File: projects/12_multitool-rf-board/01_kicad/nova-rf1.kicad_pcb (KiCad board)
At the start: 4 copper layers, 100 x 60 mm, 86 parts, among them M1 vibro, SW1 RFswitch, SW2 RFswitch, U1 STM32WB55RG, U10 ESD, U2 CC1101, U3 ST25R3916, U5 ST7565R, U6 BQ25896, U7 BQ27220, U8 LM3281, U8B LM3281, U9 loadsw, X10 BAT+NTC, X6 FFC 18p, Y1 32MHz, Y2 32.768kHz

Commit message: proj12: rename board CRL-MT1 -> NOVA-RF1 (project-wide)
Global rename across source, docs, generated schematic/board/footprint-lib,
BOM/CPL, enclosure and fab tooling. No functional change. Footprint library
prefix crl-mt1: -> nova-rf1:; silkscreen/title/fab-file names updated.
(The in-flight compact route output will be renamed when it completes.)

Co-Authored-By: Claude Opus 4.8 <noreply@anthropic.com>
Claude-Session: https://claude.ai/code/session_01Hk6s8R6up8HYVQWXd3atVk
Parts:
- ANT1: footprint crl-mt1:Antenna_Chip -> nova-rf1:Antenna_Chip
- ANT_LF: footprint crl-mt1:RFID_125k_Coil -> nova-rf1:RFID_125k_Coil
- ANT_NFC: footprint crl-mt1:NFC_Loop_Antenna -> nova-rf1:NFC_Loop_Antenna
- DA7: footprint crl-mt1:LP5562_DSBGA12 -> nova-rf1:LP5562_DSBGA12
- FLT1: footprint crl-mt1:RF_filter -> nova-rf1:RF_filter
- FLT2: footprint crl-mt1:Johanson_0310_Balun -> nova-rf1:Johanson_0310_Balun
- J_IBTN: footprint crl-mt1:iButton_Contacts -> nova-rf1:iButton_Contacts
- J_SD: footprint crl-mt1:microSD_7p -> nova-rf1:microSD_7p
- J_SWD: footprint crl-mt1:TagConnect_TC2030 -> nova-rf1:TagConnect_TC2030
- LS1: footprint crl-mt1:Speaker_2p -> nova-rf1:Speaker_2p
- M1: footprint crl-mt1:Vibro_2p -> nova-rf1:Vibro_2p
- SW1, SW2: footprint crl-mt1:RF_Switch_TSNP9 -> nova-rf1:RF_Switch_TSNP9
- U5: footprint crl-mt1:Display_ST7565_FFC -> nova-rf1:Display_ST7565_FFC
- U_IR: footprint crl-mt1:TSOP_IR_3p -> nova-rf1:TSOP_IR_3p
- VD4: footprint crl-mt1:LED_RGB_4p -> nova-rf1:LED_RGB_4p
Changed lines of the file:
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@@
 	(net 176 "unconnected-(U9-4)")
 	(net 177 "unconnected-(U9-5)")
-	(footprint "crl-mt1:Display_ST7565_FFC"
+	(footprint "nova-rf1:Display_ST7565_FFC"
 		(layer "F.Cu")
 		(at 109.739287 42.5786)
@@
 		(embedded_fonts no)
 	)
-	(footprint "crl-mt1:iButton_Contacts"
+	(footprint "nova-rf1:iButton_Contacts"
 		(layer "F.Cu")
 		(at 76.263095 43.5786)
@@
 		)
 	)
-	(footprint "crl-mt1:Speaker_2p"
+	(footprint "nova-rf1:Speaker_2p"
 		(layer "F.Cu")
 		(at 85.013095 43.0786)
@@
 		)
 	)
-	(footprint "crl-mt1:microSD_7p"
+	(footprint "nova-rf1:microSD_7p"
 		(layer "F.Cu")
 		(at 67.513095 42.6786)
@@
 		(embedded_fonts no)
 	)
-	(footprint "crl-mt1:RF_Switch_TSNP9"
+	(footprint "nova-rf1:RF_Switch_TSNP9"
 		(layer "F.Cu")
 		(at 101.318096 69.2681)
@@
 		)
 	)
-	(footprint "crl-mt1:RFID_125k_Coil"
+	(footprint "nova-rf1:RFID_125k_Coil"
 		(locked yes)
 		(layer "F.Cu")
@@
 		(embedded_fonts no)
 	)
-	(footprint "crl-mt1:LP5562_DSBGA12"
+	(footprint "nova-rf1:LP5562_DSBGA12"
 		(layer "F.Cu")
 		(at 44.396667 84.917499)
@@
 		)
 	)
-	(footprint "crl-mt1:NFC_Loop_Antenna"
+	(footprint "nova-rf1:NFC_Loop_Antenna"
 		(locked yes)
 		(layer "F.Cu")
@@
 		(embedded_fonts no)
 	)
-	(footprint "crl-mt1:Johanson_0310_Balun"
+	(footprint "nova-rf1:Johanson_0310_Balun"
 		(layer "F.Cu")
 		(at 48.900479 85.3611)
@@
 		)
 	)
-	(footprint "crl-mt1:TSOP_IR_3p"
+	(footprint "nova-rf1:TSOP_IR_3p"
 		(layer "F.Cu")
 		(at 45.915 69.8681)
@@
 		)
 	)
-	(footprint "crl-mt1:LED_RGB_4p"
+	(footprint "nova-rf1:LED_RGB_4p"
 		(layer "F.Cu")
 		(at 113.537143 69.3681)
@@
 		)
 	)
-	(footprint "crl-mt1:Antenna_Chip"
+	(footprint "nova-rf1:Antenna_Chip"
 		(locked yes)
 		(layer "F.Cu")
@@
 		(embedded_fonts no)
 	)
-	(footprint "crl-mt1:RF_filter"
+	(footprint "nova-rf1:RF_filter"
 		(layer "F.Cu")
 		(at 88.820477 68.9681)
@@
 		(embedded_fonts no)
 	)
-	(footprint "crl-mt1:RF_Switch_TSNP9"
+	(footprint "nova-rf1:RF_Switch_TSNP9"
 		(layer "F.Cu")
 		(at 107.437143 69.2681)
@@
 		)
 	)
-	(footprint "crl-mt1:Vibro_2p"
+	(footprint "nova-rf1:Vibro_2p"
 		(layer "F.Cu")
 		(at 95.183573 69.9681)
@@
 		(embedded_fonts no)
 	)
-	(footprint "crl-mt1:TagConnect_TC2030"
+	(footprint "nova-rf1:TagConnect_TC2030"
 		(locked yes)
 		(layer "F.Cu")

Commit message: proj12: elegant rounded handheld outline (no more square cut)
make_pcb.py: replace the rectangular edge with a rounded handheld silhouette
- tight top corners (R9, display/button end), generous palm-grip bottom corners
(R18), as a closed segment polygon (watertight). Nudged the GPIO header clear of
the bottom curve. check_assembly: buildable, 0 off-board.

Co-Authored-By: Claude Opus 4.8 <noreply@anthropic.com>
Claude-Session: https://claude.ai/code/session_01Hk6s8R6up8HYVQWXd3atVk
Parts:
- moved J_GPIO 4.12 mm to (124.0, 56.0)
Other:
- outline, holes or cut-outs redrawn

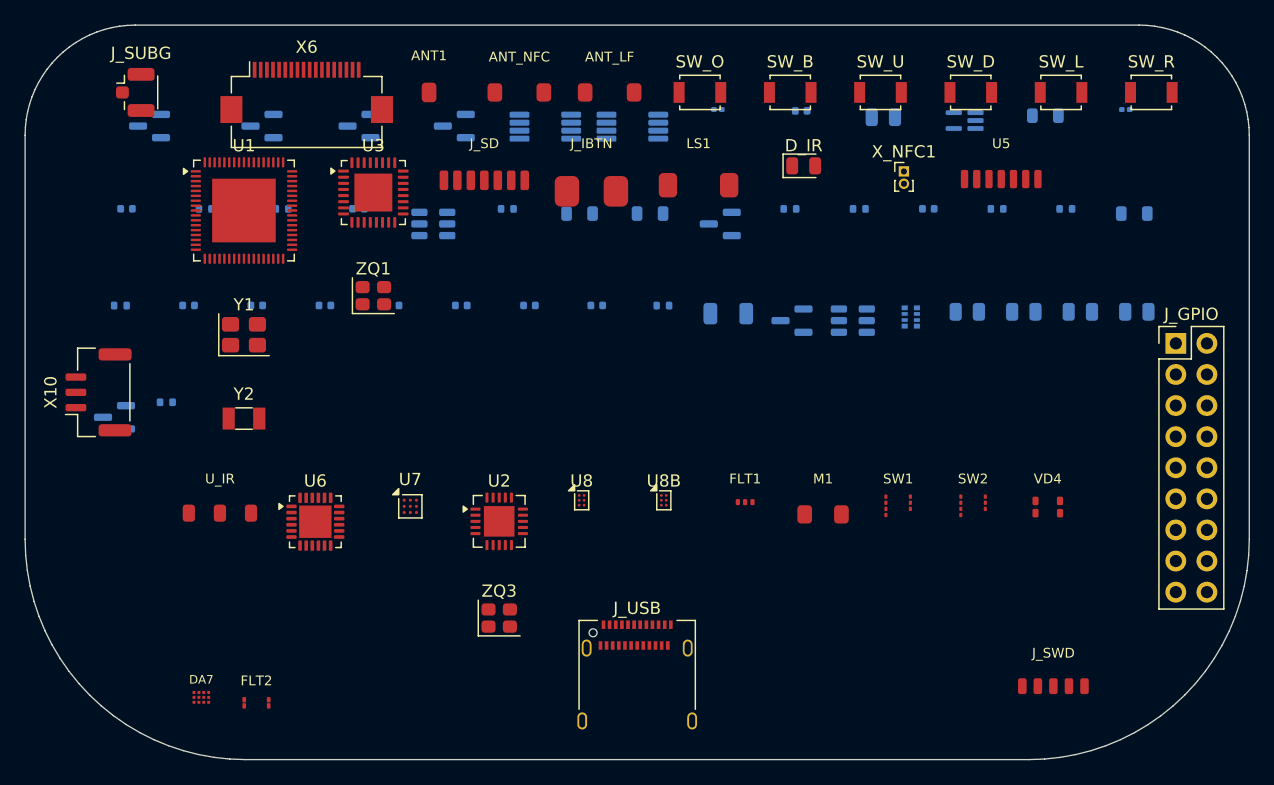
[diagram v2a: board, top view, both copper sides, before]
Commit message: proj12: level-1 design verification + fix 3 netlist bugs it caught
verify_design.py: firmware pin-map (38/38 vs Flipper F7), power+GND per IC,
decoupling, net sanity -> 32 PASS / 0 FAIL. ERC 0 errors.
Fixed: analog rail +3V3_LDO/A3V3 net-name split (op-amp rail wasn't driven);
125kHz coil driver +5V had no source (-> VSYS); added C_A3V3 decoupling.
04_docs/VERIFICATION.md documents results + how to self-check + bring-up steps.

Co-Authored-By: Claude Opus 4.8 <noreply@anthropic.com>
Claude-Session: https://claude.ai/code/session_01Hk6s8R6up8HYVQWXd3atVk
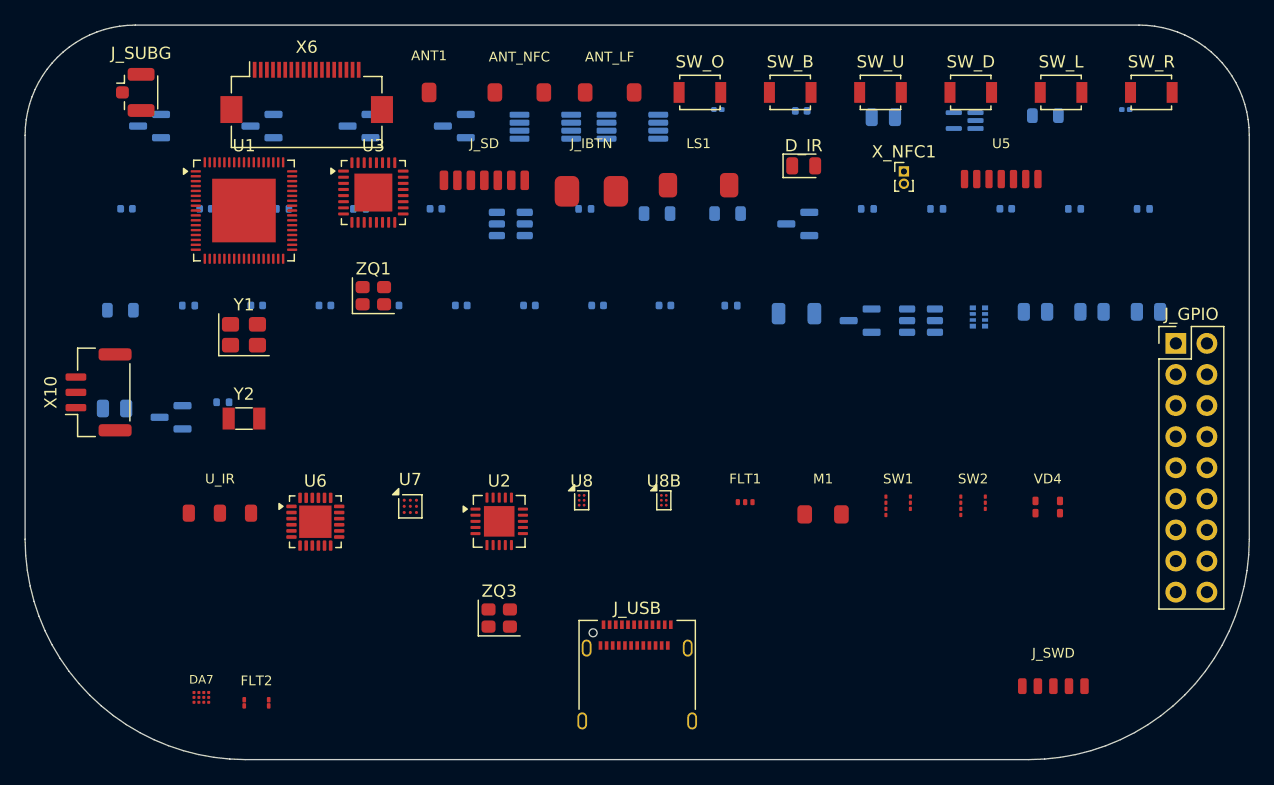
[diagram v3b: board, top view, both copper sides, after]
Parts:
- added C_A3V3: 1uF, Capacitor_SMD:C_0402_1005Metric, B.Cu at (44.7, 45.0)
- moved C10 83.9 mm to (37.3, 61.3)
- moved L_CHG 83.2 mm to (37.8, 53.3)
- moved R_CC2 6.33 mm to (104.5, 45.0)
- moved R_TS2 6.33 mm to (75.7, 45.0)
- moved C_BTST 6.33 mm to (63.6, 45.0)
- moved R_MID2 6.33 mm to (57.3, 45.0)
- moved C_CCd 6.33 mm to (110.1, 45.0)
- moved L13 6.33 mm to (81.6, 45.4)
- moved L14 6.33 mm to (87.4, 45.4)
- moved Q_SPK 6.33 mm to (93.1, 46.2)
- moved R_CC1 6.33 mm to (98.8, 45.0)
- moved R_FGO 6.33 mm to (115.7, 45.0)
- moved R_ILIM 6.33 mm to (121.3, 45.0)
- moved R_MID1 6.33 mm to (51.0, 45.0)
- moved U9 6.33 mm to (69.7, 46.2)
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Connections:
- DA8 pad 2: +3V3_LDO -> A3V3
- VT4 pad 2: +5V -> VSYS
